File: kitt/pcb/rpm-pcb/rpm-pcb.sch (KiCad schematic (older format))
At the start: 155 parts, among them J1 Screw_Terminal_01x02, Q1 NDP6020P, Q2 NDP6020P, Q3 NDP6020P, Q4 NDP6020P, Q5 NDP6020P, Q6 NDP6020P, U1 TLC5940NT, U2 TLC5940NT, U3 TLC5940NT, U4 TLC5940NT, U5 TLC5940NT, U6 TLC5940NT, U7 TLC5940NT, U8 TLC5940NT, U9 TLC5940NT

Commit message: add 12 seg led footprints
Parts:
- KEG_1_CAP_L1, KEG_1_CAP_R1, KEG_1_T1, KEG_2_T1, KEG_3_T1, KEG_4_T1, KEG_5_T1, KEG_CAP_2_L1, KEG_CAP_2_R1, KEG_CAP_3_L1, KEG_CAP_3_R1, LAGER_1_T_L1, LAGER_1_T_R1, LAGER_2_T_L1, LAGER_2_T_R1, LAGER_3_T_L1, LAGER_3_T_R1, LINE_T1: footprint (none) -> KITT-Footpads:LED_12_Segment_2.0mm_24_pin
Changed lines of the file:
@@
 F 0 "LAGER_2_T_R1" H 25578 5446 50  0000 L CNN
 F 1 "STBD01-4R8GA" H 25578 5355 50  0000 L CNN
-F 2 "" H 23800 5700 50  0001 C CNN
+F 2 "KITT-Footpads:LED_12_Segment_2.0mm_24_pin" H 23800 5700 50  0001 C CNN
 F 3 "" H 23800 5700 50  0001 C CNN
 	1    24750 5400
@@
 F 0 "LAGER_1_T_R1" H 25578 2796 50  0000 L CNN
 F 1 "STBD01-4R8GA" H 25578 2705 50  0000 L CNN
-F 2 "" H 23800 3050 50  0001 C CNN
+F 2 "KITT-Footpads:LED_12_Segment_2.0mm_24_pin" H 23800 3050 50  0001 C CNN
 F 3 "" H 23800 3050 50  0001 C CNN
 	1    24750 2750
@@
 F 0 "LINE_T1" H 9828 15596 50  0000 L CNN
 F 1 "STBD01-4R8GA" H 9828 15505 50  0000 L CNN
-F 2 "" H 8050 15850 50  0001 C CNN
+F 2 "KITT-Footpads:LED_12_Segment_2.0mm_24_pin" H 8050 15850 50  0001 C CNN
 F 3 "" H 8050 15850 50  0001 C CNN
 	1    9000 15550
@@
 F 0 "KEG_3_T1" H 7078 15596 50  0000 L CNN
 F 1 "STBD01-4R8GA" H 7078 15505 50  0000 L CNN
-F 2 "" H 5300 15850 50  0001 C CNN
+F 2 "KITT-Footpads:LED_12_Segment_2.0mm_24_pin" H 5300 15850 50  0001 C CNN
 F 3 "" H 5300 15850 50  0001 C CNN
 	1    6250 15550
@@
 F 0 "KEG_5_T1" H 9828 12346 50  0000 L CNN
 F 1 "STBD01-4R8GA" H 9828 12255 50  0000 L CNN
-F 2 "" H 8050 12600 50  0001 C CNN
+F 2 "KITT-Footpads:LED_12_Segment_2.0mm_24_pin" H 8050 12600 50  0001 C CNN
 F 3 "" H 8050 12600 50  0001 C CNN
 	1    9000 12300
@@
 F 0 "KEG_2_T1" H 7078 12346 50  0000 L CNN
 F 1 "STBD01-4R8GA" H 7078 12255 50  0000 L CNN
-F 2 "" H 5300 12600 50  0001 C CNN
+F 2 "KITT-Footpads:LED_12_Segment_2.0mm_24_pin" H 5300 12600 50  0001 C CNN
 F 3 "" H 5300 12600 50  0001 C CNN
 	1    6250 12300
@@
 F 0 "LAGER_1_T_L1" H 20650 2800 50  0000 L CNN
 F 1 "125807R" H 20800 2700 50  0000 L CNN
-F 2 "" H 21300 3050 50  0001 C CNN
+F 2 "KITT-Footpads:LED_12_Segment_2.0mm_24_pin" H 21300 3050 50  0001 C CNN
 F 3 "" H 21300 3050 50  0001 C CNN
 	1    22250 2750
@@
 F 0 "LAGER_2_T_L1" H 20650 5500 50  0000 L CNN
 F 1 "125807R" H 20800 5400 50  0000 L CNN
-F 2 "" H 21300 5700 50  0001 C CNN
+F 2 "KITT-Footpads:LED_12_Segment_2.0mm_24_pin" H 21300 5700 50  0001 C CNN
 F 3 "" H 21300 5700 50  0001 C CNN
 	1    22250 5400
@@
 F 0 "LAGER_3_T_L1" H 20650 8200 50  0000 L CNN
 F 1 "125807R" H 20800 8100 50  0000 L CNN
-F 2 "" H 21300 8450 50  0001 C CNN
+F 2 "KITT-Footpads:LED_12_Segment_2.0mm_24_pin" H 21300 8450 50  0001 C CNN
 F 3 "" H 21300 8450 50  0001 C CNN
 	1    22250 8150
@@
 F 0 "KEG_1_CAP_L1" H 23028 10696 50  0000 L CNN
 F 1 "125807R" H 23028 10605 50  0000 L CNN
-F 2 "" H 21250 10950 50  0001 C CNN
+F 2 "KITT-Footpads:LED_12_Segment_2.0mm_24_pin" H 21250 10950 50  0001 C CNN
 F 3 "" H 21250 10950 50  0001 C CNN
 	1    22200 10650
@@
 F 0 "KEG_1_CAP_R1" H 25778 10696 50  0000 L CNN
 F 1 "125807R" H 25778 10605 50  0000 L CNN
-F 2 "" H 24000 10950 50  0001 C CNN
+F 2 "KITT-Footpads:LED_12_Segment_2.0mm_24_pin" H 24000 10950 50  0001 C CNN
 F 3 "" H 24000 10950 50  0001 C CNN
 	1    24950 10650
@@
 F 0 "KEG_CAP_2_L1" H 23078 13146 50  0000 L CNN
 F 1 "125807R" H 23078 13055 50  0000 L CNN
-F 2 "" H 21300 13400 50  0001 C CNN
+F 2 "KITT-Footpads:LED_12_Segment_2.0mm_24_pin" H 21300 13400 50  0001 C CNN
 F 3 "" H 21300 13400 50  0001 C CNN
 	1    22250 13100
@@
 F 0 "KEG_CAP_3_L1" H 23078 15596 50  0000 L CNN
 F 1 "125807R" H 23078 15505 50  0000 L CNN
-F 2 "" H 21300 15850 50  0001 C CNN
+F 2 "KITT-Footpads:LED_12_Segment_2.0mm_24_pin" H 21300 15850 50  0001 C CNN
 F 3 "" H 21300 15850 50  0001 C CNN
 	1    22250 15550
@@
 F 0 "KEG_CAP_3_R1" H 25828 15596 50  0000 L CNN
 F 1 "125807R" H 25828 15505 50  0000 L CNN
-F 2 "" H 24050 15850 50  0001 C CNN
+F 2 "KITT-Footpads:LED_12_Segment_2.0mm_24_pin" H 24050 15850 50  0001 C CNN
 F 3 "" H 24050 15850 50  0001 C CNN
 	1    25000 15550
@@
 F 0 "KEG_CAP_2_R1" H 25828 13146 50  0000 L CNN
 F 1 "125807R" H 25828 13055 50  0000 L CNN
-F 2 "" H 24050 13400 50  0001 C CNN
+F 2 "KITT-Footpads:LED_12_Segment_2.0mm_24_pin" H 24050 13400 50  0001 C CNN
 F 3 "" H 24050 13400 50  0001 C CNN
 	1    25000 13100
@@
 F 0 "KEG_4_T1" H 9828 9196 50  0000 L CNN
 F 1 "STBD01-4R8GA" H 9828 9105 50  0000 L CNN
-F 2 "" H 8050 9450 50  0001 C CNN
+F 2 "KITT-Footpads:LED_12_Segment_2.0mm_24_pin" H 8050 9450 50  0001 C CNN
 F 3 "" H 8050 9450 50  0001 C CNN
 	1    9000 9150
@@
 F 0 "KEG_1_T1" H 7078 9196 50  0000 L CNN
 F 1 "STBD01-4R8GA" H 7078 9105 50  0000 L CNN
-F 2 "" H 5300 9450 50  0001 C CNN
+F 2 "KITT-Footpads:LED_12_Segment_2.0mm_24_pin" H 5300 9450 50  0001 C CNN
 F 3 "" H 5300 9450 50  0001 C CNN
 	1    6250 9150
@@
 F 0 "LAGER_3_T_R1" H 25578 8196 50  0000 L CNN
 F 1 "STBD01-4R8GA" H 25578 8105 50  0000 L CNN
-F 2 "" H 23800 8450 50  0001 C CNN
+F 2 "KITT-Footpads:LED_12_Segment_2.0mm_24_pin" H 23800 8450 50  0001 C CNN
 F 3 "" H 23800 8450 50  0001 C CNN
 	1    24750 8150

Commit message: add footpad for logic level shifter
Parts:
- LVL1, LVL2, LVL3: footprint (none) -> KITT-Footpads:LVL_5V_3V3
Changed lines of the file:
@@
 F 0 "LVL3" V 19004 17938 50  0000 L CNN
 F 1 "LVL_5V_3V3" V 19095 17938 50  0000 L CNN
-F 2 "" H 19050 17550 50  0001 C CNN
+F 2 "KITT-Footpads:LVL_5V_3V3" H 19050 17550 50  0001 C CNN
 F 3 "" H 19050 17550 50  0001 C CNN
 	1    19050 17550
@@
 F 0 "LVL2" V 3254 17938 50  0000 L CNN
 F 1 "LVL_5V_3V3" V 3345 17938 50  0000 L CNN
-F 2 "" H 3300 17550 50  0001 C CNN
+F 2 "KITT-Footpads:LVL_5V_3V3" H 3300 17550 50  0001 C CNN
 F 3 "" H 3300 17550 50  0001 C CNN
 	1    3300 17550
@@
 F 0 "LVL1" H 3450 21475 50  0000 C CNN
 F 1 "LVL_5V_3V3" H 3450 21384 50  0000 C CNN
-F 2 "" H 3450 20950 50  0001 C CNN
+F 2 "KITT-Footpads:LVL_5V_3V3" H 3450 20950 50  0001 C CNN
 F 3 "" H 3450 20950 50  0001 C CNN
 	1    3450 20950
@@
 	25550 7850 25700 7850
 Connection ~ 25550 7850
+Wire Wire Line
+	2050 20850 3100 20850
+Wire Wire Line
+	2050 20950 3100 20950
+$Comp
+L Connector:Screw_Terminal_01x02 J1
+U 1 1 61430C56
+P 1850 20850
+F 0 "J1" H 1768 21067 50  0000 C CNN
+F 1 "Screw_Terminal_01x02" H 1768 20976 50  0000 C CNN
+F 2 "KITT-Footpads:5mm_Screw_Terminal_01x02" H 1850 20850 50  0001 C CNN
+F 3 "~" H 1850 20850 50  0001 C CNN
+	1    1850 20850
+	-1   0    0    -1
+$EndComp
 Wire Bus Line
 	21150 10250 21850 10250
@@
 Wire Bus Line
 	5400 16700 17300 16700
-Wire Wire Line
-	2050 20850 3100 20850
-Wire Wire Line
-	2050 20950 3100 20950
-$Comp
-L Connector:Screw_Terminal_01x02 J1
-U 1 1 61430C56
-P 1850 20850
-F 0 "J1" H 1768 21067 50  0000 C CNN
-F 1 "Screw_Terminal_01x02" H 1768 20976 50  0000 C CNN
-F 2 "KITT-Footpads:5mm_Screw_Terminal_01x02" H 1850 20850 50  0001 C CNN
-F 3 "~" H 1850 20850 50  0001 C CNN
-	1    1850 20850
-	-1   0    0    -1
-$EndComp
 $EndSCHEMATC

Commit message: fixed coupling caps and blank resistors
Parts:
- removed R20, R21, R22, R24, R26, R28, R30: 10K, Resistor_THT:R_Axial_DIN0207_L6.3mm_D2.5mm_P10.16mm_Horizontal, symbol Device:R
- added MH1, MH2, MH3, MH4, MH5, MH6, MH7, MH8: MountingHole, MountingHole:MountingHole_3.2mm_M3, symbol Mechanical:MountingHole
- added NT1, NT10, NT11, NT12, NT13, NT2, NT3, NT4, NT5, NT6, NT7, NT8, NT9: Net-Tie_3_Tee, NetTie:NetTie-3_THT_Pad0.3mm, symbol Device:Net-Tie_3_Tee
- added PEG1, PEG2, PEG3, PEG4: MountingHole, MountingHole:MountingHole_5.3mm_M5, symbol Mechanical:MountingHole
- added THRU1, THRU2: MountingHole, MountingHole:MountingHole_6.4mm_M6, symbol Mechanical:MountingHole
- C13: value 1uF -> 100nF
- C9: value 100nF -> 1uF
- renumbered J1 to J2, R6 to R1, R15 to R10, R16 to R11, R17 to R12, R18 to R13, R1 to R14, R2 to R15, R3 to R16, R4 to R17, R5 to R18, R7 to R2, R23 to R20, R25 to R21, R27 to R22, R29 to R23, R8 to R3, R9 to R4, R10 to R5, R11 to R6, R12 to R7, R13 to R8, R14 to R9
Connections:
- net +5V: now also NT10.3, NT11.3, NT12.3, NT13.3, NT2.3, NT3.3, NT4.3, NT5.3, NT6.3, NT7.3, NT9.3; no longer C1.1, C10.1, C11.1, C12.1, C13.1, C2.1, C3.1, C4.1, C5.1, C6.1, C7.1, C8.1, C9.1, TTGO1.1 (5V), TTGO2.1 (5V), U1.21 (VCC), U2.21 (VCC), U3.21 (VCC), U4.21 (VCC), U5.21 (VCC), U6.21 (VCC), U7.21 (VCC), U8.21 (VCC), U9.21 (VCC)
- net BLANK: no longer R19.2
- net BLANK_2: now also R19.2
- net GND: now also C2.1, C9.1; no longer C2.2, C9.2
- new net: NT8.1, TTGO2.1 (5V)
- new net: NT3.1, U1.21 (VCC)
- new net: C2.2, NT2.1
- new net: C3.1, NT3.2
- new net: NT4.1, U2.21 (VCC)
- new net: NT5.1, U3.21 (VCC)
- new net: NT10.1, U6.21 (VCC)
- new net: NT7.1, U5.21 (VCC)
- new net: C1.1, NT1.3
- new net: NT1.1, TTGO1.1 (5V)
- new net: NT6.1, U4.21 (VCC)
- new net: NT11.1, U7.21 (VCC)
- new net: NT1.2, NT2.2
- new net: NT12.1, U8.21 (VCC)
- new net: NT13.1, U9.21 (VCC)
- new net: C9.2, NT9.1
- new net: C8.1, NT8.3
- new net: NT8.2, NT9.2
- new net: C4.1, NT4.2
- new net: C5.1, NT5.2
- new net: C6.1, NT6.2
- new net: C7.1, NT7.2
- new net: C10.1, NT10.2
- new net: C11.1, NT11.2
- new net: C12.1, NT12.2
- new net: C13.1, NT13.2
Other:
- moved on the sheet: C1, C2, R13

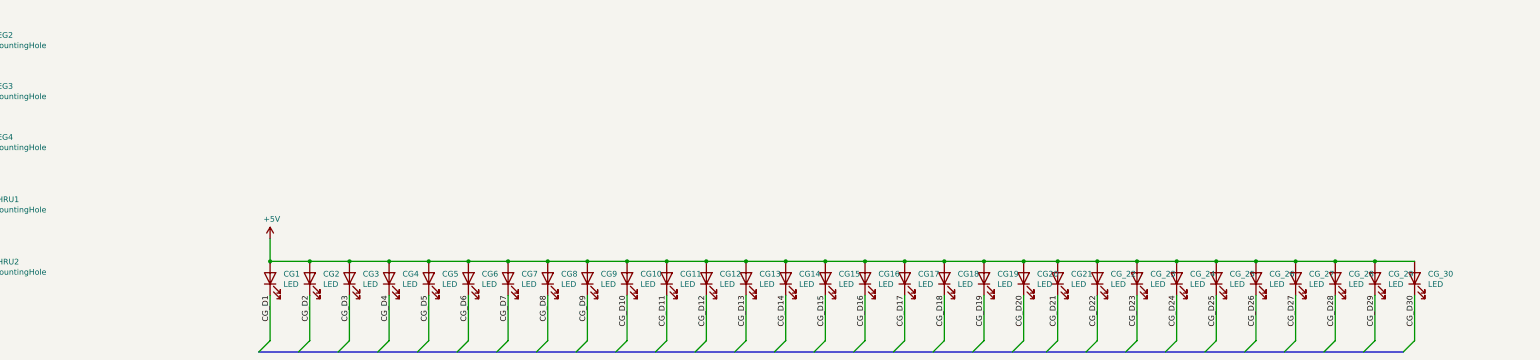
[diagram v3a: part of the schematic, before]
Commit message: placed rpm leds
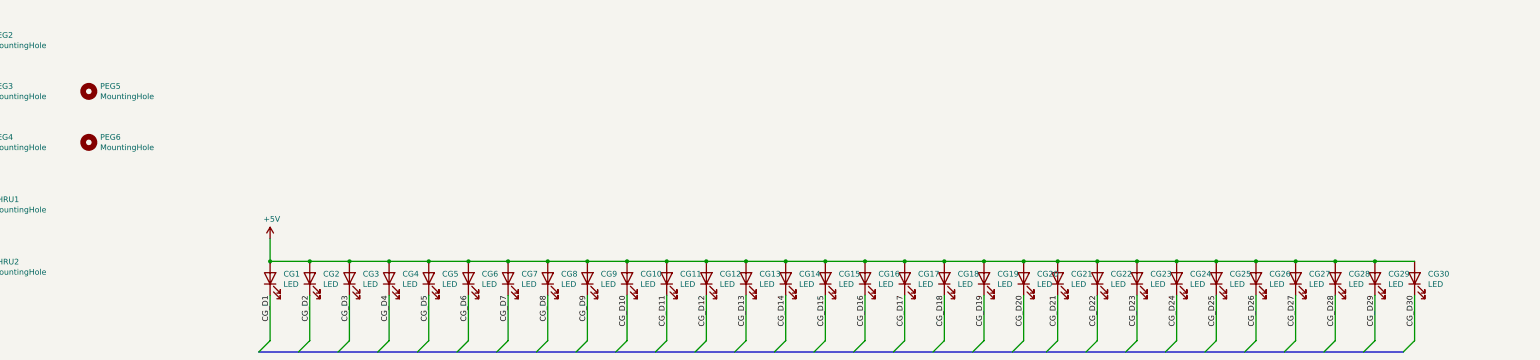
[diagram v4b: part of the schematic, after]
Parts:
- added PEG5, PEG6: MountingHole, MountingHole:MountingHole_5.3mm_M5, symbol Mechanical:MountingHole
- renumbered CG_22 to CG22, CG_23 to CG23, CG_24 to CG24, CG_25 to CG25, CG_26 to CG26, CG_27 to CG27, CG_28 to CG28, CG_29 to CG29, CG_30 to CG30
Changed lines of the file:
@@
 Connection ~ 12050 3650
 $Comp
-L Device:LED CG_30
+L Device:LED CG30
 U 1 1 612893CF
 P 14850 3800
-F 0 "CG_30" V 14889 3682 50  0000 R CNN
+F 0 "CG30" V 14889 3682 50  0000 R CNN
 F 1 "LED" V 14798 3682 50  0000 R CNN
 F 2 "KITT-Footpads:Flangeless_LED" H 14850 3800 50  0001 C CNN
@@
 $EndComp
 $Comp
-L Device:LED CG_29
+L Device:LED CG29
 U 1 1 612893CE
 P 14500 3800
-F 0 "CG_29" V 14539 3682 50  0000 R CNN
+F 0 "CG29" V 14539 3682 50  0000 R CNN
 F 1 "LED" V 14448 3682 50  0000 R CNN
 F 2 "KITT-Footpads:Flangeless_LED" H 14500 3800 50  0001 C CNN
@@
 $EndComp
 $Comp
-L Device:LED CG_28
+L Device:LED CG28
 U 1 1 6112DC7B
 P 14150 3800
-F 0 "CG_28" V 14189 3682 50  0000 R CNN
+F 0 "CG28" V 14189 3682 50  0000 R CNN
 F 1 "LED" V 14098 3682 50  0000 R CNN
 F 2 "KITT-Footpads:Flangeless_LED" H 14150 3800 50  0001 C CNN
@@
 $EndComp
 $Comp
-L Device:LED CG_27
+L Device:LED CG27
 U 1 1 612893C4
 P 13800 3800
-F 0 "CG_27" V 13839 3682 50  0000 R CNN
+F 0 "CG27" V 13839 3682 50  0000 R CNN
 F 1 "LED" V 13748 3682 50  0000 R CNN
 F 2 "KITT-Footpads:Flangeless_LED" H 13800 3800 50  0001 C CNN
@@
 $EndComp
 $Comp
-L Device:LED CG_26
+L Device:LED CG26
 U 1 1 612893C3
 P 13450 3800
-F 0 "CG_26" V 13489 3682 50  0000 R CNN
+F 0 "CG26" V 13489 3682 50  0000 R CNN
 F 1 "LED" V 13398 3682 50  0000 R CNN
 F 2 "KITT-Footpads:Flangeless_LED" H 13450 3800 50  0001 C CNN
@@
 $EndComp
 $Comp
-L Device:LED CG_25
+L Device:LED CG25
 U 1 1 612893C2
 P 13100 3800
-F 0 "CG_25" V 13139 3682 50  0000 R CNN
+F 0 "CG25" V 13139 3682 50  0000 R CNN
 F 1 "LED" V 13048 3682 50  0000 R CNN
 F 2 "KITT-Footpads:Flangeless_LED" H 13100 3800 50  0001 C CNN
@@
 $EndComp
 $Comp
-L Device:LED CG_24
+L Device:LED CG24
 U 1 1 612893BE
 P 12750 3800
-F 0 "CG_24" V 12789 3682 50  0000 R CNN
+F 0 "CG24" V 12789 3682 50  0000 R CNN
 F 1 "LED" V 12698 3682 50  0000 R CNN
 F 2 "KITT-Footpads:Flangeless_LED" H 12750 3800 50  0001 C CNN
@@
 $EndComp
 $Comp
-L Device:LED CG_23
+L Device:LED CG23
 U 1 1 61118DB3
 P 12400 3800
-F 0 "CG_23" V 12439 3682 50  0000 R CNN
+F 0 "CG23" V 12439 3682 50  0000 R CNN
 F 1 "LED" V 12348 3682 50  0000 R CNN
 F 2 "KITT-Footpads:Flangeless_LED" H 12400 3800 50  0001 C CNN
@@
 $EndComp
 $Comp
-L Device:LED CG_22
+L Device:LED CG22
 U 1 1 6110EE01
 P 12050 3800
-F 0 "CG_22" V 12089 3682 50  0000 R CNN
+F 0 "CG22" V 12089 3682 50  0000 R CNN
 F 1 "LED" V 11998 3682 50  0000 R CNN
 F 2 "KITT-Footpads:Flangeless_LED" H 12050 3800 50  0001 C CNN
@@
 	1    0    0    -1
 $EndComp
+$Comp
+L Mechanical:MountingHole PEG5
+U 1 1 6168010C
+P 3150 2150
+F 0 "PEG5" H 3250 2196 50  0000 L CNN
+F 1 "MountingHole" H 3250 2105 50  0000 L CNN
+F 2 "MountingHole:MountingHole_5.3mm_M5" H 3150 2150 50  0001 C CNN
+F 3 "~" H 3150 2150 50  0001 C CNN
+	1    3150 2150
+	1    0    0    -1
+$EndComp
+$Comp
+L Mechanical:MountingHole PEG6
+U 1 1 61680112
+P 3150 2600
+F 0 "PEG6" H 3250 2646 50  0000 L CNN
+F 1 "MountingHole" H 3250 2555 50  0000 L CNN
+F 2 "MountingHole:MountingHole_5.3mm_M5" H 3150 2600 50  0001 C CNN
+F 3 "~" H 3150 2600 50  0001 C CNN
+	1    3150 2600
+	1    0    0    -1
+$EndComp

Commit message: added extra cg led
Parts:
- added CG0: LED, KITT-Footpads:Flangeless_LED, symbol Device:LED
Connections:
- net +5V: now also CG0.2 (A)
- net CG_D0: now reaches U2.28 (OUT0)
- net CG_D0: now also CG0.1 (K)
- no-connect marks 41 -> 40
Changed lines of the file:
@@
 Text Label 16000 17600 1    50   ~ 0
 KEG_T_R_YD1
-NoConn ~ 8100 17600
 NoConn ~ 10700 17600
 Wire Wire Line
@@
 	5450 3650 5100 3650
 Connection ~ 5450 3650
-Wire Wire Line
-	5100 3650 4750 3650
 Connection ~ 5100 3650
 Wire Wire Line
@@
 $EndComp
 $Comp
-L power:GND #PWR?
+L power:GND #PWR0105
 U 1 1 6242AD6E
 P 23200 21750
-F 0 "#PWR?" H 23200 21500 50  0001 C CNN
+F 0 "#PWR0105" H 23200 21500 50  0001 C CNN
 F 1 "GND" H 23205 21577 50  0000 C CNN
 F 2 "" H 23200 21750 50  0001 C CNN
@@
 $EndComp
 $Comp
-L power:GND #PWR?
+L power:GND #PWR0108
 U 1 1 6242AD7A
 P 22600 22150
-F 0 "#PWR?" H 22600 21900 50  0001 C CNN
+F 0 "#PWR0108" H 22600 21900 50  0001 C CNN
 F 1 "GND" H 22605 21977 50  0000 C CNN
 F 2 "" H 22600 22150 50  0001 C CNN
@@
 $EndComp
 $Comp
-L power:+5V #PWR?
+L power:+5V #PWR0110
 U 1 1 6242AD86
 P 22800 21850
-F 0 "#PWR?" H 22800 21700 50  0001 C CNN
+F 0 "#PWR0110" H 22800 21700 50  0001 C CNN
 F 1 "+5V" V 22815 21978 50  0000 L CNN
 F 2 "" H 22800 21850 50  0001 C CNN
@@
 $EndComp
 $Comp
-L power:GND #PWR?
+L power:GND #PWR0113
 U 1 1 6242AD8C
 P 22500 21650
-F 0 "#PWR?" H 22500 21400 50  0001 C CNN
+F 0 "#PWR0113" H 22500 21400 50  0001 C CNN
 F 1 "GND" V 22505 21522 50  0000 R CNN
 F 2 "" H 22500 21650 50  0001 C CNN
@@
 	22500 21150 23350 21150
 $Comp
-L power:+5V #PWR?
+L power:+5V #PWR0116
 U 1 1 6358E142
 P 23050 20700
-F 0 "#PWR?" H 23050 20550 50  0001 C CNN
+F 0 "#PWR0116" H 23050 20550 50  0001 C CNN
 F 1 "+5V" H 23065 20873 50  0000 C CNN
 F 2 "" H 23050 20700 50  0001 C CNN
@@
 $EndComp
 $Comp
-L power:GND #PWR?
+L power:GND #PWR0119
 U 1 1 64D4A370
 P 7600 18600
-F 0 "#PWR?" H 7600 18350 50  0001 C CNN
+F 0 "#PWR0119" H 7600 18350 50  0001 C CNN
 F 1 "GND" H 7605 18427 50  0000 C CNN
 F 2 "" H 7600 18600 50  0001 C CNN
@@
 $EndComp
 $Comp
-L power:+5V #PWR?
+L power:+5V #PWR0123
 U 1 1 64D4A37C
 P 7700 18200
-F 0 "#PWR?" H 7700 18050 50  0001 C CNN
+F 0 "#PWR0123" H 7700 18050 50  0001 C CNN
 F 1 "+5V" H 7715 18373 50  0000 C CNN
 F 2 "" H 7700 18200 50  0001 C CNN
@@
 $EndComp
 $Comp
-L power:GND #PWR?
+L power:GND #PWR0124
 U 1 1 64E69AAA
 P 10200 18600
-F 0 "#PWR?" H 10200 18350 50  0001 C CNN
+F 0 "#PWR0124" H 10200 18350 50  0001 C CNN
 F 1 "GND" H 10205 18427 50  0000 C CNN
 F 2 "" H 10200 18600 50  0001 C CNN
@@
 $EndComp
 $Comp
-L power:+5V #PWR?
+L power:+5V #PWR0125
 U 1 1 64E69AB6
 P 10300 18200
-F 0 "#PWR?" H 10300 18050 50  0001 C CNN
+F 0 "#PWR0125" H 10300 18050 50  0001 C CNN
 F 1 "+5V" H 10315 18373 50  0000 C CNN
 F 2 "" H 10300 18200 50  0001 C CNN
@@
 $EndComp
 $Comp
-L power:GND #PWR?
+L power:GND #PWR0126
 U 1 1 64F89048
 P 12800 18600
-F 0 "#PWR?" H 12800 18350 50  0001 C CNN
+F 0 "#PWR0126" H 12800 18350 50  0001 C CNN
 F 1 "GND" H 12805 18427 50  0000 C CNN
 F 2 "" H 12800 18600 50  0001 C CNN
@@
 $EndComp
 $Comp
-L power:+5V #PWR?
+L power:+5V #PWR0133
 U 1 1 64F89054
 P 12900 18200
-F 0 "#PWR?" H 12900 18050 50  0001 C CNN
+F 0 "#PWR0133" H 12900 18050 50  0001 C CNN
 F 1 "+5V" H 12915 18373 50  0000 C CNN
 F 2 "" H 12900 18200 50  0001 C CNN
@@
 $EndComp
 $Comp
-L power:GND #PWR?
+L power:GND #PWR0134
 U 1 1 650A9038
 P 15400 18600
-F 0 "#PWR?" H 15400 18350 50  0001 C CNN
+F 0 "#PWR0134" H 15400 18350 50  0001 C CNN
 F 1 "GND" H 15405 18427 50  0000 C CNN
 F 2 "" H 15400 18600 50  0001 C CNN
@@
 $EndComp
 $Comp
-L power:+5V #PWR?
+L power:+5V #PWR0135
 U 1 1 650A9044
 P 15500 18200
-F 0 "#PWR?" H 15500 18050 50  0001 C CNN
+F 0 "#PWR0135" H 15500 18050 50  0001 C CNN
 F 1 "+5V" H 15515 18373 50  0000 C CNN
 F 2 "" H 15500 18200 50  0001 C CNN
@@
 $EndComp
 $Comp
-L power:GND #PWR?
+L power:GND #PWR0136
 U 1 1 651C9618
 P 21000 18600
-F 0 "#PWR?" H 21000 18350 50  0001 C CNN
+F 0 "#PWR0136" H 21000 18350 50  0001 C CNN
 F 1 "GND" H 21005 18427 50  0000 C CNN
 F 2 "" H 21000 18600 50  0001 C CNN
@@
 $EndComp
 $Comp
-L power:+5V #PWR?
+L power:+5V #PWR0139
 U 1 1 651C9624
 P 21100 18200
-F 0 "#PWR?" H 21100 18050 50  0001 C CNN
+F 0 "#PWR0139" H 21100 18050 50  0001 C CNN
 F 1 "+5V" H 21115 18373 50  0000 C CNN
 F 2 "" H 21100 18200 50  0001 C CNN
@@
 $EndComp
 $Comp
-L power:GND #PWR?
+L power:GND #PWR0140
 U 1 1 652E8E70
 P 23600 18600
-F 0 "#PWR?" H 23600 18350 50  0001 C CNN
+F 0 "#PWR0140" H 23600 18350 50  0001 C CNN
 F 1 "GND" H 23605 18427 50  0000 C CNN
 F 2 "" H 23600 18600 50  0001 C CNN
@@
 $EndComp
 $Comp
-L power:+5V #PWR?
+L power:+5V #PWR0142
 U 1 1 652E8E7C
 P 23700 18200
-F 0 "#PWR?" H 23700 18050 50  0001 C CNN
+F 0 "#PWR0142" H 23700 18050 50  0001 C CNN
 F 1 "+5V" H 23715 18373 50  0000 C CNN
 F 2 "" H 23700 18200 50  0001 C CNN
@@
 $EndComp
 $Comp
-L power:GND #PWR?
+L power:GND #PWR0143
 U 1 1 65406222
 P 26200 18600
-F 0 "#PWR?" H 26200 18350 50  0001 C CNN
+F 0 "#PWR0143" H 26200 18350 50  0001 C CNN
 F 1 "GND" H 26205 18427 50  0000 C CNN
 F 2 "" H 26200 18600 50  0001 C CNN
@@
 $EndComp
 $Comp
-L power:+5V #PWR?
+L power:+5V #PWR0144
 U 1 1 6540622E
 P 26300 18200
-F 0 "#PWR?" H 26300 18050 50  0001 C CNN
+F 0 "#PWR0144" H 26300 18050 50  0001 C CNN
 F 1 "+5V" H 26315 18373 50  0000 C CNN
 F 2 "" H 26300 18200 50  0001 C CNN
@@
 $EndComp
 $Comp
-L power:GND #PWR?
+L power:GND #PWR0147
 U 1 1 65526BA4
 P 28800 18600
-F 0 "#PWR?" H 28800 18350 50  0001 C CNN
+F 0 "#PWR0147" H 28800 18350 50  0001 C CNN
 F 1 "GND" H 28805 18427 50  0000 C CNN
 F 2 "" H 28800 18600 50  0001 C CNN
@@
 $EndComp
 $Comp
-L power:+5V #PWR?
+L power:+5V #PWR0157
 U 1 1 65526BB0
 P 28900 18200
-F 0 "#PWR?" H 28900 18050 50  0001 C CNN
+F 0 "#PWR0157" H 28900 18050 50  0001 C CNN
 F 1 "+5V" H 28915 18373 50  0000 C CNN
 F 2 "" H 28900 18200 50  0001 C CNN
@@
 	1    0    0    -1
 $EndComp
+Wire Wire Line
+	4450 4350 4450 3950
+Entry Wire Line
+	4350 4450 4450 4350
+Text Label 4450 3950 3    50   ~ 0
+CG_D0
+$Comp
+L Device:LED CG0
+U 1 1 61CBA73E
+P 4450 3800
+F 0 "CG0" V 4489 3682 50  0000 R CNN
+F 1 "LED" V 4398 3682 50  0000 R CNN
+F 2 "KITT-Footpads:Flangeless_LED" H 4450 3800 50  0001 C CNN
+F 3 "~" H 4450 3800 50  0001 C CNN
+	1    4450 3800
+	0    -1   -1   0
+$EndComp
+Wire Wire Line
+	4450 3650 4750 3650
+Connection ~ 4800 3650
+Wire Wire Line
+	4800 3650 4750 3650
+Entry Wire Line
+	8000 16700 8100 16800
+Wire Wire Line
+	8100 16800 8100 17600
+Wire Wire Line
+	4750 3650 5100 3650
 Wire Bus Line
 	21150 10250 21850 10250
@@
 	5450 9950 7100 9950
 Wire Bus Line
-	4650 4450 14750 4450
+	4350 4450 14750 4450
 Wire Bus Line
 	7650 19900 17300 19900
@@
 Wire Bus Line
 	5400 16700 17300 16700
+Text Label 8100 17600 1    50   ~ 0
+CG_D0
 $EndSCHEMATC
